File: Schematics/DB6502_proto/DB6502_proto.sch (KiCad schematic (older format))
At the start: 22 parts, among them SW1 Reset, U1 DS1813, U10 28C256, U11 22V10C, U2 74AC32, U3 65C02S, U4 74AC04, U5 62256, U6 74HC74, U7 74AC08, U8 62256, U9 74AC138, X1 14MHz

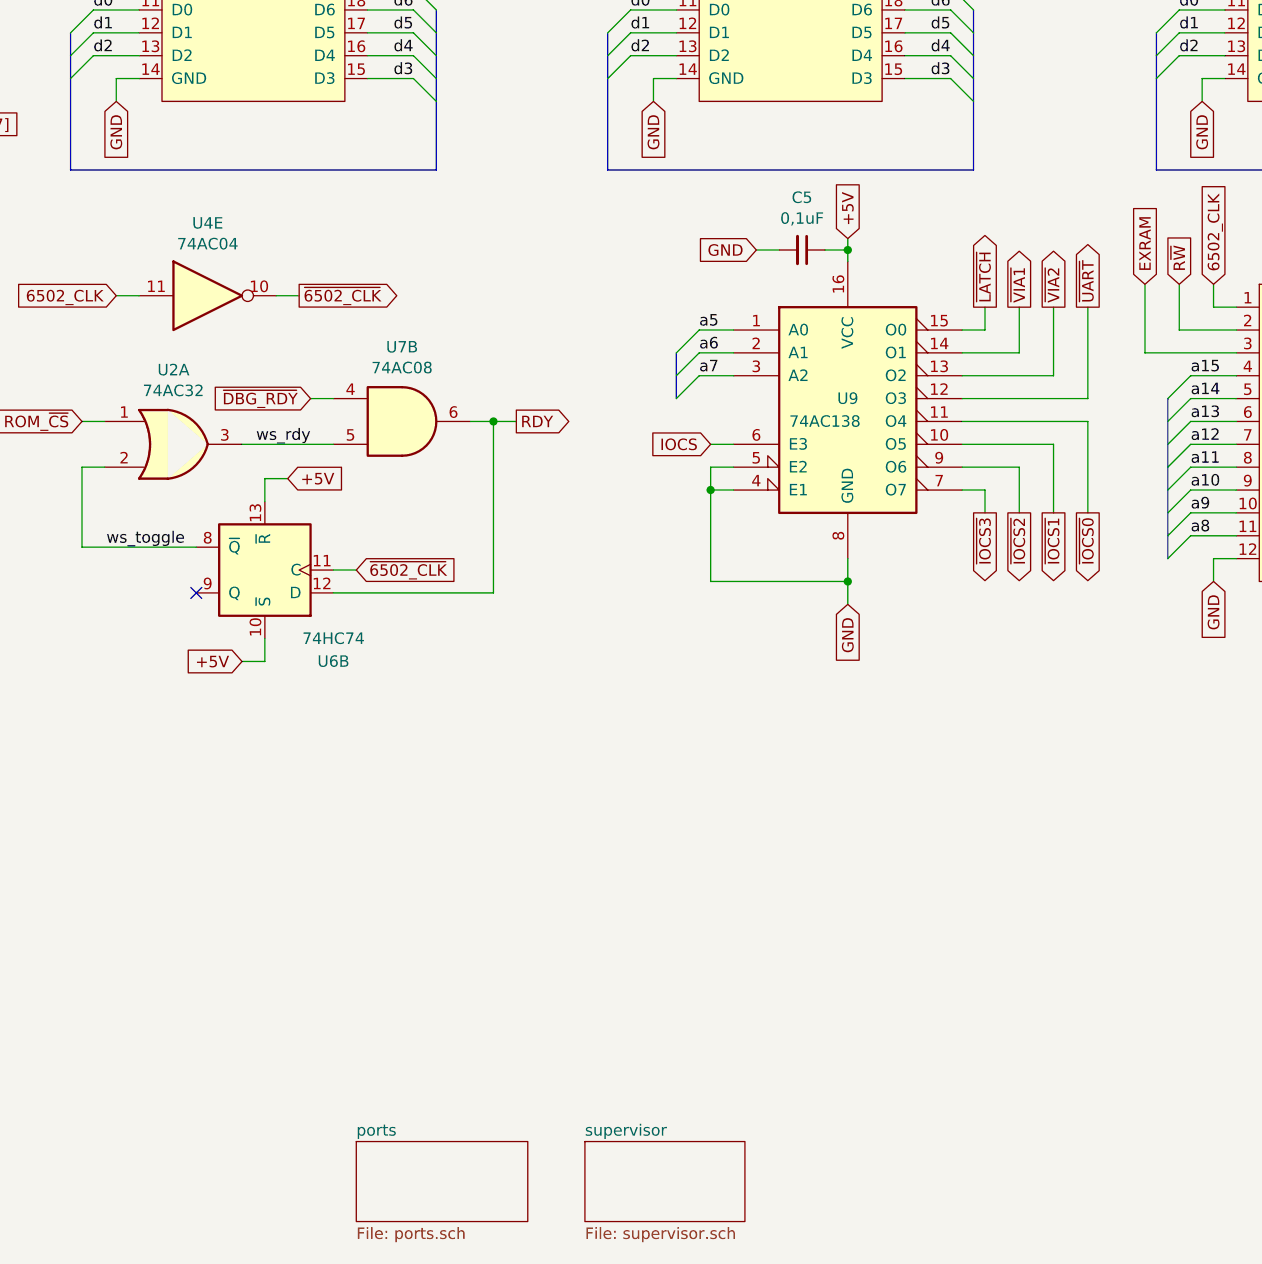
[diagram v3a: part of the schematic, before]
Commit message: Added I/O schematics page with DUART chip
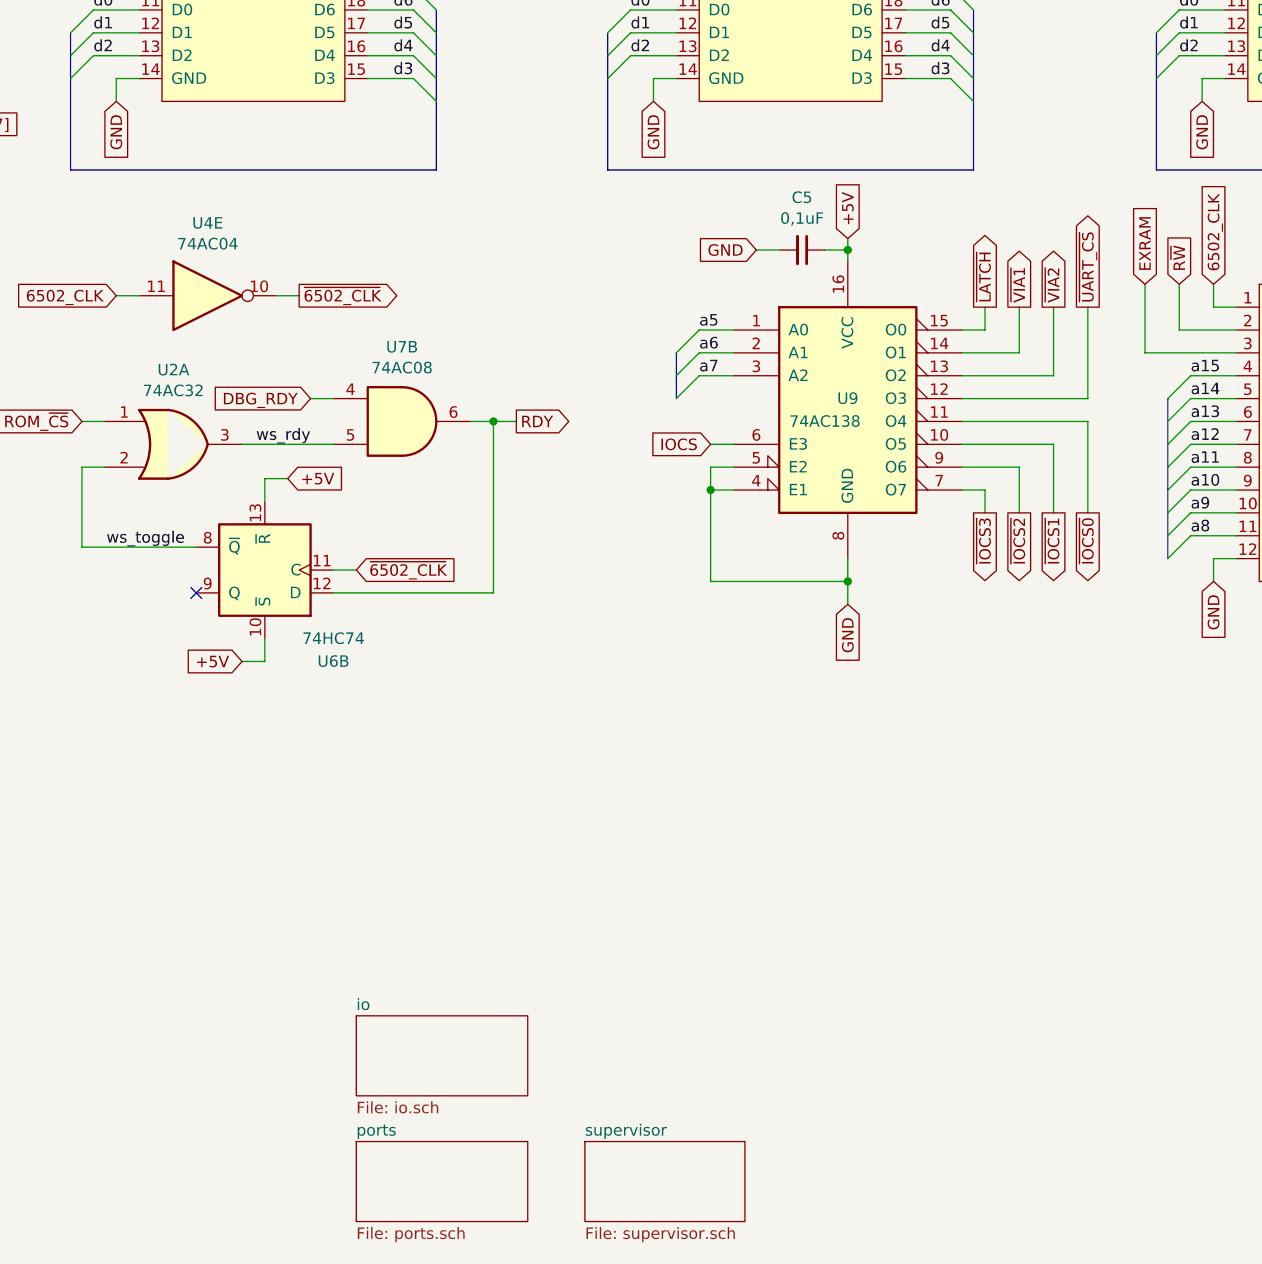
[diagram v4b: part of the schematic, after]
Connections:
- net ~DBG_RDY renamed DBG_RDY
- net ~UART renamed ~UART_CS
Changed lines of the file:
@@
 $Descr A4 11693 8268
 encoding utf-8
-Sheet 1 3
+Sheet 1 4
 Title "DB6502 Hobby Computer Version 2"
 Date "2020-10-13"
@@
 	8150 3850 7750 3850
 Text GLabel 8300 3550 1    50   Output ~ 0
-~UART
+~UART_CS
 Wire Wire Line
 	8300 3550 8300 3950
@@
 $EndComp
 Text GLabel 4900 3950 0    50   Input ~ 0
-~DBG_RDY
+DBG_RDY
 Wire Wire Line
 	4900 3950 5000 3950
@@
 	1    0    0    -1
 $EndComp
+$Sheet
+S 5100 6650 750  350
+U 5F910E81
+F0 "io" 50
+F1 "io.sch" 50
+$EndSheet
 Wire Bus Line
 	6500 3750 6500 3950
